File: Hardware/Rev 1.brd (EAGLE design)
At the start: 50 x 31 mm, 16 parts, among them IC1 LM5069MM-2, T1 AUIRFS8409-7P

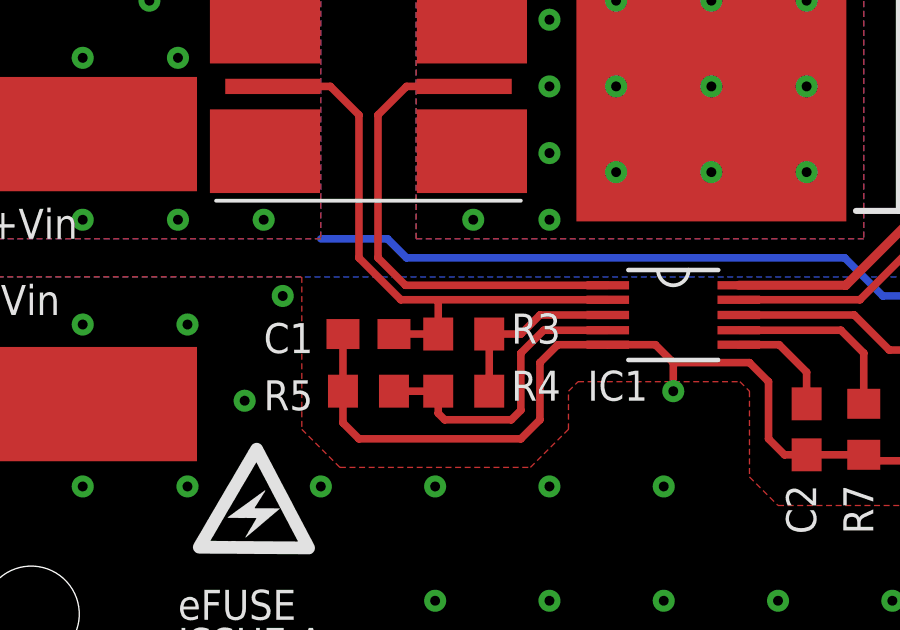
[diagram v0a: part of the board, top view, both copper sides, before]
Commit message: Add image and current limit maths.
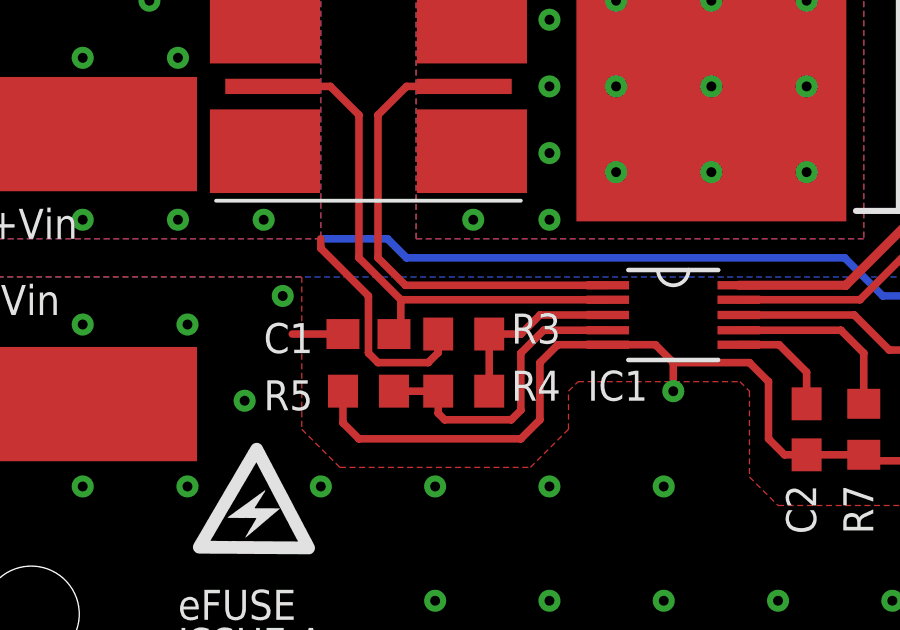
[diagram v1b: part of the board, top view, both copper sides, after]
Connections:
- net VIN: now also R3.2
- net VIN_K: no longer R3.2
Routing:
- net VIN: track 23.4 -> 31.1 mm
- net VIN_K: track 19.5 -> 18.1 mm
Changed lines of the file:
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@@
 <setting verticaltext="up"/>
 </settings>
-<grid distance="0.005" unitdist="mm" unit="mm" style="lines" multiple="1" display="yes" altdistance="0.0125" altunitdist="inch" altunit="inch"/>
+<grid distance="0.025" unitdist="inch" unit="inch" style="lines" multiple="1" display="yes" altdistance="0.0125" altunitdist="inch" altunit="inch"/>
 <layers>
 <layer number="1" name="Top" color="4" fill="1" visible="yes" active="yes"/>
@@
 <via x="8.89" y="22.5425" extent="1-16" drill="0.3302"/>
 <via x="7.9375" y="24.4475" extent="1-16" drill="0.3302"/>
+<contactref element="R3" pad="2"/>
+<wire x1="15.5575" y1="12.3825" x2="15.24" y2="12.7" width="0.254" layer="1"/>
+<wire x1="15.24" y1="12.7" x2="15.24" y2="14.605" width="0.254" layer="1"/>
+<wire x1="17.565" y1="13.335" x2="17.565" y2="12.716134375" width="0.254" layer="1"/>
+<wire x1="17.565" y1="12.716134375" x2="17.231365625" y2="12.3825" width="0.254" layer="1"/>
+<wire x1="17.231365625" y1="12.3825" x2="15.5575" y2="12.3825" width="0.254" layer="1"/>
+<wire x1="15.24" y1="14.605" x2="13.6525" y2="16.1925" width="0.254" layer="1"/>
+<wire x1="13.6525" y1="16.1925" x2="13.6525" y2="16.51" width="0.254" layer="1"/>
 </signal>
 <signal name="VSEN">
@@
 </polygon>
 <via x="12.3825" y="14.605" extent="1-16" drill="0.3302"/>
-<wire x1="14.39" y1="11.43" x2="14.39" y2="13.335" width="0.254" layer="1"/>
 <wire x1="14.39" y1="11.43" x2="14.39" y2="10.375" width="0.254" layer="1"/>
 <wire x1="14.39" y1="10.375" x2="14.9225" y2="9.8425" width="0.254" layer="1"/>
@@
 <via x="25.0825" y="8.255" extent="1-16" drill="0.3302"/>
 <via x="13.6525" y="8.255" extent="1-16" drill="0.3302"/>
+<wire x1="14.39" y1="13.335" x2="12.7" y2="13.335" width="0.254" layer="1"/>
 </signal>
 <signal name="GATE_DRIVE">
@@
 <contactref element="IC1" pad="2"/>
 <contactref element="C1" pad="1"/>
-<contactref element="R3" pad="2"/>
 <wire x1="14.9225" y1="20.6375" x2="14.9225" y2="15.875" width="0.254" layer="1"/>
 <wire x1="16.3195" y1="14.478" x2="14.9225" y2="15.875" width="0.254" layer="1"/>
 <contactref element="R1" pad="BK"/>
-<wire x1="23.2156" y1="14.478" x2="17.565" y2="14.478" width="0.254" layer="1"/>
-<wire x1="17.565" y1="14.478" x2="16.3195" y2="14.478" width="0.254" layer="1"/>
-<wire x1="17.565" y1="13.335" x2="17.565" y2="14.478" width="0.254" layer="1"/>
-<wire x1="16.09" y1="13.335" x2="17.565" y2="13.335" width="0.254" layer="1"/>
+<wire x1="23.2156" y1="14.478" x2="16.3195" y2="14.478" width="0.254" layer="1"/>
 <wire x1="12.045" y1="21.59" x2="13.97" y2="21.59" width="0.254" layer="1"/>
 <wire x1="13.97" y1="21.59" x2="14.9225" y2="20.6375" width="0.254" layer="1"/>
+<wire x1="16.3195" y1="14.478" x2="16.3195" y2="13.5645" width="0.254" layer="1"/>
+<wire x1="16.3195" y1="13.5645" x2="16.09" y2="13.335" width="0.254" layer="1"/>
 </signal>
 </signals>
